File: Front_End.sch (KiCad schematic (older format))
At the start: 17 parts, among them SW2 JS202011SCQN, SW3 JS202011SCQN, U5 SKY65366-21, U6 BMI-S-101

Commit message: setup netclasses and added more footprints
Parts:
- RV1: footprint Resistors_SMD:R_0402 -> SFUSat-Radio:TC33_SMD
- SW2, SW3: footprint SFUSat-Radio:JS2020_SMD -> SFUSat-Radio:JS2020_TH
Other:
- note added: "RF Shield\n"
- note added: "Select external control of enable\n and VPC or tie internally to high \nor low respective."
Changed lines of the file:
@@
 F 0 "RV1" H 4650 5750 50  0000 C CNN
 F 1 "POT" H 4650 5850 50  0000 C CNN
-F 2 "Resistors_SMD:R_0402" H 4650 5850 50  0001 C CNN
+F 2 "SFUSat-Radio:TC33_SMD" H 4650 5850 50  0001 C CNN
 F 3 "" H 4650 5850 50  0000 C CNN
 	1    4650 5850
@@
 F 0 "SW2" H 3800 5750 60  0000 C CNN
 F 1 "JS202011SCQN" H 3600 6300 60  0000 C CNN
-F 2 "SFUSat-Radio:JS2020_SMD" H 3600 6150 60  0001 C CNN
+F 2 "SFUSat-Radio:JS2020_TH" H 3600 6150 60  0001 C CNN
 F 3 "" H 3600 6150 60  0000 C CNN
 	1    3600 6150
@@
 F 0 "SW3" H 6100 5750 60  0000 C CNN
 F 1 "JS202011SCQN" H 5900 6300 60  0000 C CNN
-F 2 "SFUSat-Radio:JS2020_SMD" H 5900 6150 60  0001 C CNN
+F 2 "SFUSat-Radio:JS2020_TH" H 5900 6150 60  0001 C CNN
 F 3 "" H 5900 6150 60  0000 C CNN
 	1    5900 6150
@@
 	8100 5000 8000 5000
 Connection ~ 8000 5000
+Text Notes 3000 7000 0    60   ~ 0
+Select external control of enable\n and VPC or tie internally to high \nor low respective.
+Text Notes 7500 5850 0    60   ~ 0
+RF Shield\n
 $EndSCHEMATC

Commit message: fixed filesystem
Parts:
- C28, C29, C30, L2: footprint (none) -> Capacitors_SMD:C_0402
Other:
- note added: "LNA and PA can be bypassed if\n BYP in pulled HIGH. Good as a \nkill switch to high power output.\n"
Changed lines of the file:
@@
 F 0 "C29" V 7300 3200 50  0000 C CNN
 F 1 "3pF" V 7600 3200 50  0000 C CNN
-F 2 "" H 7488 3050 50  0001 C CNN
+F 2 "Capacitors_SMD:C_0402" H 7488 3050 50  0001 C CNN
 F 3 "" H 7450 3200 50  0000 C CNN
 	1    7450 3200
@@
 F 0 "C28" H 7075 3450 50  0000 L CNN
 F 1 "8.2pF" H 7075 3250 50  0000 L CNN
-F 2 "" H 7088 3200 50  0001 C CNN
+F 2 "Capacitors_SMD:C_0402" H 7088 3200 50  0001 C CNN
 F 3 "" H 7050 3350 50  0000 C CNN
 	1    7050 3350
@@
 F 0 "C30" H 7875 3450 50  0000 L CNN
 F 1 "8.2pF" H 7875 3250 50  0000 L CNN
-F 2 "" H 7888 3200 50  0001 C CNN
+F 2 "Capacitors_SMD:C_0402" H 7888 3200 50  0001 C CNN
 F 3 "" H 7850 3350 50  0000 C CNN
 	1    7850 3350
@@
 F 0 "L2" V 7400 2825 50  0000 C CNN
 F 1 "12nH" V 7550 2825 50  0000 C CNN
-F 2 "" H 7450 2825 50  0001 C CNN
+F 2 "Capacitors_SMD:C_0402" H 7450 2825 50  0001 C CNN
 F 3 "" H 7450 2825 50  0000 C CNN
 	1    7450 2825
@@
 Text Label 2900 6400 0    60   ~ 0
 EN
-Text Notes 2600 4900 0    60   ~ 0
+Text Notes 2100 3600 0    60   ~ 0
 TR and BYP should not be \npulled high if EN is pulled low
 $Comp
@@
 Text Notes 7500 5850 0    60   ~ 0
 RF Shield\n
+Text Notes 5150 6850 0    60   ~ 0
+LNA and PA can be bypassed if\n BYP in pulled HIGH. Good as a \nkill switch to high power output.\n
 $EndSCHEMATC

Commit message: added some test points
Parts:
- removed SW2: JS202011SCQN, SFUSat-Radio:JS2020_TH, symbol JS202011SCQN
- added P? (x2): CONN_01X03, symbol CONN_01X03
- added W?: TEST_1P, symbol TEST_1P
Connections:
- wire segments 40 -> 41
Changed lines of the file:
@@
 Text HLabel 8200 3200 2    60   Input ~ 0
 ANT
-Text HLabel 4100 6100 2    60   Input ~ 0
+Text HLabel 4100 6400 2    60   Input ~ 0
 PA_ADJ
 Text HLabel 6500 4000 2    60   Input ~ 0
@@
 Wire Wire Line
 	4700 3350 3800 3350
-Text HLabel 4100 6350 2    60   Input ~ 0
+Text HLabel 3300 6400 2    60   Input ~ 0
 EN
 Text Notes 3400 2775 0    60   ~ 0
@@
 Text Label 3800 3700 0    60   ~ 0
 VPC
-Text Label 2900 6150 0    60   ~ 0
+Text Label 4350 6300 2    60   ~ 0
 VPC
 Text HLabel 4800 5850 2    60   Input ~ 0
@@
 	0    1    1    0
 $EndComp
-$Comp
-L JS202011SCQN SW2
-U 1 1 587E3043
-P 3600 6150
-F 0 "SW2" H 3800 5750 60  0000 C CNN
-F 1 "JS202011SCQN" H 3600 6300 60  0000 C CNN
-F 2 "SFUSat-Radio:JS2020_TH" H 3600 6150 60  0001 C CNN
-F 3 "" H 3600 6150 60  0000 C CNN
-	1    3600 6150
-	1    0    0    -1
-$EndComp
-Wire Wire Line
-	3100 6150 2900 6150
 Wire Wire Line
 	4650 6200 4100 6200
-Text HLabel 4100 6450 2    60   Input ~ 0
+Text HLabel 3300 6200 2    60   Input ~ 0
 3V3
 Text Label 3800 3350 0    60   ~ 0
 EN
-Wire Wire Line
-	3100 6400 2900 6400
-Text Label 2900 6400 0    60   ~ 0
+Text Label 3450 6300 2    60   ~ 0
 EN
 Text Notes 2100 3600 0    60   ~ 0
@@
 Text Notes 5150 6850 0    60   ~ 0
 LNA and PA can be bypassed if\n BYP in pulled HIGH. Good as a \nkill switch to high power output.\n
+$Comp
+L CONN_01X03 P?
+U 1 1 5881FCF5
+P 3900 6300
+F 0 "P?" H 3900 6500 50  0000 C CNN
+F 1 "CONN_01X03" V 4000 6300 50  0000 C CNN
+F 2 "" H 3900 6300 50  0000 C CNN
+F 3 "" H 3900 6300 50  0000 C CNN
+	1    3900 6300
+	-1   0    0    1
+$EndComp
+$Comp
+L CONN_01X03 P?
+U 1 1 5881FDBC
+P 3100 6300
+F 0 "P?" H 3100 6500 50  0000 C CNN
+F 1 "CONN_01X03" V 3200 6300 50  0000 C CNN
+F 2 "" H 3100 6300 50  0000 C CNN
+F 3 "" H 3100 6300 50  0000 C CNN
+	1    3100 6300
+	-1   0    0    1
+$EndComp
+Wire Wire Line
+	4100 6300 4350 6300
+Wire Wire Line
+	3300 6300 3450 6300
+$Comp
+L TEST_1P W?
+U 1 1 58821DE8
+P 4300 6050
+F 0 "W?" H 4300 6320 50  0000 C CNN
+F 1 "TEST_1P" H 4300 6250 50  0000 C CNN
+F 2 "" H 4500 6050 50  0000 C CNN
+F 3 "" H 4500 6050 50  0000 C CNN
+	1    4300 6050
+	1    0    0    -1
+$EndComp
+Wire Wire Line
+	4300 6050 4300 6200
+Connection ~ 4300 6200
 $EndSCHEMATC

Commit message: layed out all components
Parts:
- removed U6: BMI-S-101, SFUSat-Radio:BMI-S-101, symbol BMI-S-101
- P2, P3: renamed from P?; footprint (none) -> Socket_Strips:Socket_Strip_Straight_1x03
- W3: renamed from W?; footprint (none) -> Measurement_Points:Measurement_Point_Round-SMD-Pad_Small
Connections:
- wire segments 41 -> 37
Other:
- note removed: "RF Shield\n"
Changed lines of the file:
@@
 $EndComp
 $Comp
-L GND #PWR028
+L GND #PWR027
 U 1 1 58719F72
 P 5500 4650
-F 0 "#PWR028" H 5500 4400 50  0001 C CNN
+F 0 "#PWR027" H 5500 4400 50  0001 C CNN
 F 1 "GND" H 5500 4500 50  0000 C CNN
 F 2 "" H 5500 4650 50  0000 C CNN
@@
 $EndComp
 $Comp
-L GND #PWR029
+L GND #PWR028
 U 1 1 5871BAFA
 P 5750 2550
-F 0 "#PWR029" H 5750 2300 50  0001 C CNN
+F 0 "#PWR028" H 5750 2300 50  0001 C CNN
 F 1 "GND" H 5750 2400 50  0000 C CNN
 F 2 "" H 5750 2550 50  0000 C CNN
@@
 $EndComp
 $Comp
-L GND #PWR030
+L GND #PWR029
 U 1 1 5871BB16
 P 6050 2550
-F 0 "#PWR030" H 6050 2300 50  0001 C CNN
+F 0 "#PWR029" H 6050 2300 50  0001 C CNN
 F 1 "GND" H 6050 2400 50  0000 C CNN
 F 2 "" H 6050 2550 50  0000 C CNN
@@
 $EndComp
 $Comp
-L GND #PWR031
+L GND #PWR030
 U 1 1 5871BB32
 P 6350 2550
-F 0 "#PWR031" H 6350 2300 50  0001 C CNN
+F 0 "#PWR030" H 6350 2300 50  0001 C CNN
 F 1 "GND" H 6350 2400 50  0000 C CNN
 F 2 "" H 6350 2550 50  0000 C CNN
@@
 $EndComp
 $Comp
-L GND #PWR032
+L GND #PWR031
 U 1 1 5871BD81
 P 5150 2550
-F 0 "#PWR032" H 5150 2300 50  0001 C CNN
+F 0 "#PWR031" H 5150 2300 50  0001 C CNN
 F 1 "GND" H 5150 2400 50  0000 C CNN
 F 2 "" H 5150 2550 50  0000 C CNN
@@
 $EndComp
 $Comp
-L GND #PWR033
+L GND #PWR032
 U 1 1 5871BDA1
 P 4850 2550
-F 0 "#PWR033" H 4850 2300 50  0001 C CNN
+F 0 "#PWR032" H 4850 2300 50  0001 C CNN
 F 1 "GND" H 4850 2400 50  0000 C CNN
 F 2 "" H 4850 2550 50  0000 C CNN
@@
 	7050 2825 7050 3200
 $Comp
-L GND #PWR034
+L GND #PWR033
 U 1 1 5871C376
 P 7050 3600
-F 0 "#PWR034" H 7050 3350 50  0001 C CNN
+F 0 "#PWR033" H 7050 3350 50  0001 C CNN
 F 1 "GND" H 7050 3450 50  0000 C CNN
 F 2 "" H 7050 3600 50  0000 C CNN
@@
 $EndComp
 $Comp
-L GND #PWR035
+L GND #PWR034
 U 1 1 5871C39E
 P 7850 3600
-F 0 "#PWR035" H 7850 3350 50  0001 C CNN
+F 0 "#PWR034" H 7850 3350 50  0001 C CNN
 F 1 "GND" H 7850 3450 50  0000 C CNN
 F 2 "" H 7850 3600 50  0000 C CNN
@@
 $EndComp
 $Comp
-L GND #PWR036
+L GND #PWR035
 U 1 1 5871CA19
 P 4500 4400
-F 0 "#PWR036" H 4500 4150 50  0001 C CNN
+F 0 "#PWR035" H 4500 4150 50  0001 C CNN
 F 1 "GND" H 4500 4250 50  0000 C CNN
 F 2 "" H 4500 4400 50  0000 C CNN
@@
 $EndComp
 $Comp
-L GND #PWR037
+L GND #PWR036
 U 1 1 5871CD23
 P 4150 4050
-F 0 "#PWR037" H 4150 3800 50  0001 C CNN
+F 0 "#PWR036" H 4150 3800 50  0001 C CNN
 F 1 "GND" H 4150 3900 50  0000 C CNN
 F 2 "" H 4150 4050 50  0000 C CNN
@@
 $EndComp
 $Comp
-L GND #PWR038
+L GND #PWR037
 U 1 1 587C3C45
 P 4650 6600
-F 0 "#PWR038" H 4650 6350 50  0001 C CNN
+F 0 "#PWR037" H 4650 6350 50  0001 C CNN
 F 1 "GND" H 4650 6450 50  0000 C CNN
 F 2 "" H 4650 6600 50  0000 C CNN
@@
 3V3
 $Comp
-L GND #PWR039
+L GND #PWR038
 U 1 1 58829BDE
 P 6400 6100
-F 0 "#PWR039" H 6400 5850 50  0001 C CNN
+F 0 "#PWR038" H 6400 5850 50  0001 C CNN
 F 1 "GND" H 6400 5950 50  0000 C CNN
 F 2 "" H 6400 6100 50  0000 C CNN
@@
 	0    -1   -1   0
 $EndComp
-$Comp
-L BMI-S-101 U6
-U 1 1 5882B6C7
-P 7600 4850
-F 0 "U6" H 7750 4050 60  0000 C CNN
-F 1 "BMI-S-101" H 7600 5000 60  0000 C CNN
-F 2 "SFUSat-Radio:BMI-S-101" H 7600 4850 60  0001 C CNN
-F 3 "" H 7600 4850 60  0000 C CNN
-	1    7600 4850
-	1    0    0    -1
-$EndComp
-$Comp
-L GND #PWR040
-U 1 1 5882B8A8
-P 8100 5000
-F 0 "#PWR040" H 8100 4750 50  0001 C CNN
-F 1 "GND" H 8100 4850 50  0000 C CNN
-F 2 "" H 8100 5000 50  0000 C CNN
-F 3 "" H 8100 5000 50  0000 C CNN
-	1    8100 5000
-	0    -1   -1   0
-$EndComp
-Wire Wire Line
-	8000 4850 8000 5550
-Wire Wire Line
-	8000 4950 8000 5250
-Connection ~ 8000 5050
-Connection ~ 8000 4950
-Connection ~ 8000 5150
-Connection ~ 8000 5250
-Wire Wire Line
-	8000 5350 8000 5450
-Connection ~ 8000 5450
-Connection ~ 8000 5350
-Wire Wire Line
-	8100 5000 8000 5000
-Connection ~ 8000 5000
 Text Notes 3000 7000 0    60   ~ 0
 Select external control of enable\n and VPC or tie internally to high \nor low respective.
-Text Notes 7500 5850 0    60   ~ 0
-RF Shield\n
 Text Notes 5150 6850 0    60   ~ 0
 LNA and PA can be bypassed if\n BYP in pulled HIGH. Good as a \nkill switch to high power output.\n
 $Comp
-L CONN_01X03 P?
+L CONN_01X03 P3
 U 1 1 5881FCF5
 P 3900 6300
-F 0 "P?" H 3900 6500 50  0000 C CNN
+F 0 "P3" H 3900 6500 50  0000 C CNN
 F 1 "CONN_01X03" V 4000 6300 50  0000 C CNN
-F 2 "" H 3900 6300 50  0000 C CNN
+F 2 "Socket_Strips:Socket_Strip_Straight_1x03" H 3900 6300 50  0001 C CNN
 F 3 "" H 3900 6300 50  0000 C CNN
 	1    3900 6300
@@
 $EndComp
 $Comp
-L CONN_01X03 P?
+L CONN_01X03 P2
 U 1 1 5881FDBC
 P 3100 6300
-F 0 "P?" H 3100 6500 50  0000 C CNN
+F 0 "P2" H 3100 6500 50  0000 C CNN
 F 1 "CONN_01X03" V 3200 6300 50  0000 C CNN
-F 2 "" H 3100 6300 50  0000 C CNN
+F 2 "Socket_Strips:Socket_Strip_Straight_1x03" H 3100 6300 50  0001 C CNN
 F 3 "" H 3100 6300 50  0000 C CNN
 	1    3100 6300
@@
 	3300 6300 3450 6300
 $Comp
-L TEST_1P W?
+L TEST_1P W3
 U 1 1 58821DE8
 P 4300 6050
-F 0 "W?" H 4300 6320 50  0000 C CNN
+F 0 "W3" H 4300 6320 50  0000 C CNN
 F 1 "TEST_1P" H 4300 6250 50  0000 C CNN
-F 2 "" H 4500 6050 50  0000 C CNN
+F 2 "Measurement_Points:Measurement_Point_Round-SMD-Pad_Small" H 4500 6050 50  0001 C CNN
 F 3 "" H 4500 6050 50  0000 C CNN
 	1    4300 6050

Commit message: Checked changes from botched commit
-R5 and R6 are gone as desired
-C4 changed from 10 nF to 100 nF looks good
-Split up nets between pins 27 and 28 so each have their own dedicated
capacitor
-Added C9 to pin 28 and forward annotated it into the layout
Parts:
- RV1: symbol POT -> POT-RESCUE-SFUSat-Radio
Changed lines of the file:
@@
 EESchema Schematic File Version 2
+LIBS:SFUSat-Radio-rescue
 LIBS:power
 LIBS:device
@@
 $EndComp
 $Comp
-L GND #PWR027
+L GND #PWR32
 U 1 1 58719F72
 P 5500 4650
-F 0 "#PWR027" H 5500 4400 50  0001 C CNN
+F 0 "#PWR32" H 5500 4400 50  0001 C CNN
 F 1 "GND" H 5500 4500 50  0000 C CNN
 F 2 "" H 5500 4650 50  0000 C CNN
@@
 $EndComp
 $Comp
-L GND #PWR028
+L GND #PWR33
 U 1 1 5871BAFA
 P 5750 2550
-F 0 "#PWR028" H 5750 2300 50  0001 C CNN
+F 0 "#PWR33" H 5750 2300 50  0001 C CNN
 F 1 "GND" H 5750 2400 50  0000 C CNN
 F 2 "" H 5750 2550 50  0000 C CNN
@@
 $EndComp
 $Comp
-L GND #PWR029
+L GND #PWR34
 U 1 1 5871BB16
 P 6050 2550
-F 0 "#PWR029" H 6050 2300 50  0001 C CNN
+F 0 "#PWR34" H 6050 2300 50  0001 C CNN
 F 1 "GND" H 6050 2400 50  0000 C CNN
 F 2 "" H 6050 2550 50  0000 C CNN
@@
 $EndComp
 $Comp
-L GND #PWR030
+L GND #PWR35
 U 1 1 5871BB32
 P 6350 2550
-F 0 "#PWR030" H 6350 2300 50  0001 C CNN
+F 0 "#PWR35" H 6350 2300 50  0001 C CNN
 F 1 "GND" H 6350 2400 50  0000 C CNN
 F 2 "" H 6350 2550 50  0000 C CNN
@@
 $EndComp
 $Comp
-L GND #PWR031
+L GND #PWR31
 U 1 1 5871BD81
 P 5150 2550
-F 0 "#PWR031" H 5150 2300 50  0001 C CNN
+F 0 "#PWR31" H 5150 2300 50  0001 C CNN
 F 1 "GND" H 5150 2400 50  0000 C CNN
 F 2 "" H 5150 2550 50  0000 C CNN
@@
 $EndComp
 $Comp
-L GND #PWR032
+L GND #PWR30
 U 1 1 5871BDA1
 P 4850 2550
-F 0 "#PWR032" H 4850 2300 50  0001 C CNN
+F 0 "#PWR30" H 4850 2300 50  0001 C CNN
 F 1 "GND" H 4850 2400 50  0000 C CNN
 F 2 "" H 4850 2550 50  0000 C CNN
@@
 	7050 2825 7050 3200
 $Comp
-L GND #PWR033
+L GND #PWR37
 U 1 1 5871C376
 P 7050 3600
-F 0 "#PWR033" H 7050 3350 50  0001 C CNN
+F 0 "#PWR37" H 7050 3350 50  0001 C CNN
 F 1 "GND" H 7050 3450 50  0000 C CNN
 F 2 "" H 7050 3600 50  0000 C CNN
@@
 $EndComp
 $Comp
-L GND #PWR034
+L GND #PWR38
 U 1 1 5871C39E
 P 7850 3600
-F 0 "#PWR034" H 7850 3350 50  0001 C CNN
+F 0 "#PWR38" H 7850 3350 50  0001 C CNN
 F 1 "GND" H 7850 3450 50  0000 C CNN
 F 2 "" H 7850 3600 50  0000 C CNN
@@
 $EndComp
 $Comp
-L GND #PWR035
+L GND #PWR28
 U 1 1 5871CA19
 P 4500 4400
-F 0 "#PWR035" H 4500 4150 50  0001 C CNN
+F 0 "#PWR28" H 4500 4150 50  0001 C CNN
 F 1 "GND" H 4500 4250 50  0000 C CNN
 F 2 "" H 4500 4400 50  0000 C CNN
@@
 $EndComp
 $Comp
-L GND #PWR036
+L GND #PWR27
 U 1 1 5871CD23
 P 4150 4050
-F 0 "#PWR036" H 4150 3800 50  0001 C CNN
+F 0 "#PWR27" H 4150 3800 50  0001 C CNN
 F 1 "GND" H 4150 3900 50  0000 C CNN
 F 2 "" H 4150 4050 50  0000 C CNN
@@
 $EndComp
 $Comp
-L GND #PWR037
+L GND #PWR29
 U 1 1 587C3C45
 P 4650 6600
-F 0 "#PWR037" H 4650 6350 50  0001 C CNN
+F 0 "#PWR29" H 4650 6350 50  0001 C CNN
 F 1 "GND" H 4650 6450 50  0000 C CNN
 F 2 "" H 4650 6600 50  0000 C CNN
@@
 3V3
 $Comp
-L POT RV1
+L POT-RESCUE-SFUSat-Radio RV1
 U 1 1 587CA745
 P 4650 5850
@@
 3V3
 $Comp
-L GND #PWR038
+L GND #PWR36
 U 1 1 58829BDE
 P 6400 6100
-F 0 "#PWR038" H 6400 5850 50  0001 C CNN
+F 0 "#PWR36" H 6400 5850 50  0001 C CNN
 F 1 "GND" H 6400 5950 50  0000 C CNN
 F 2 "" H 6400 6100 50  0000 C CNN

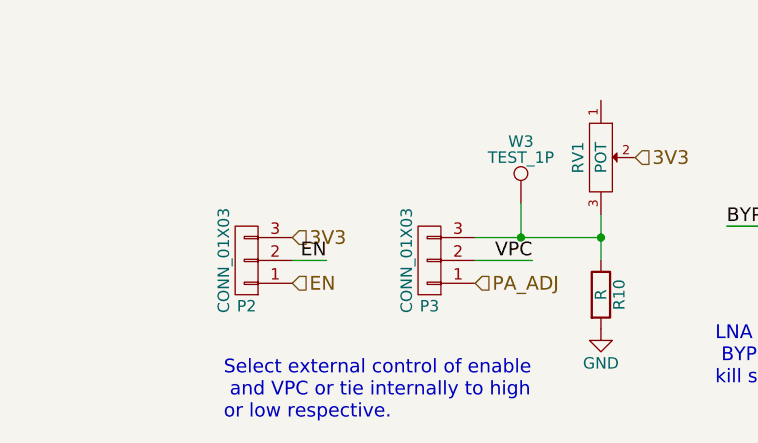
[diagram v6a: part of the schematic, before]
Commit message: added power connector, nets connected in layout
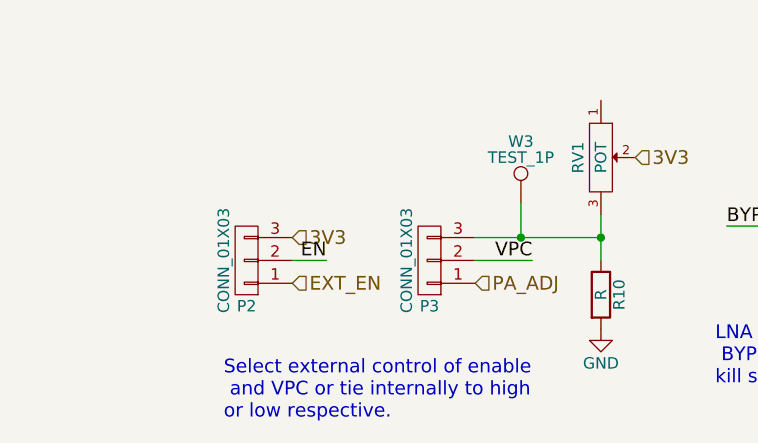
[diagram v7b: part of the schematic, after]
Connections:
- net EN: no longer P2.1 (P1)
- new net EXT_EN: P2.1 (P1)
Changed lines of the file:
@@
 $EndComp
 $Comp
-L GND #PWR026
+L GND #PWR027
 U 1 1 58719F72
 P 5500 4650
-F 0 "#PWR026" H 5500 4400 50  0001 C CNN
+F 0 "#PWR027" H 5500 4400 50  0001 C CNN
 F 1 "GND" H 5500 4500 50  0000 C CNN
 F 2 "" H 5500 4650 50  0000 C CNN
@@
 $EndComp
 $Comp
-L GND #PWR027
+L GND #PWR028
 U 1 1 5871BAFA
 P 5750 2550
-F 0 "#PWR027" H 5750 2300 50  0001 C CNN
+F 0 "#PWR028" H 5750 2300 50  0001 C CNN
 F 1 "GND" H 5750 2400 50  0000 C CNN
 F 2 "" H 5750 2550 50  0000 C CNN
@@
 $EndComp
 $Comp
-L GND #PWR028
+L GND #PWR029
 U 1 1 5871BB16
 P 6050 2550
-F 0 "#PWR028" H 6050 2300 50  0001 C CNN
+F 0 "#PWR029" H 6050 2300 50  0001 C CNN
 F 1 "GND" H 6050 2400 50  0000 C CNN
 F 2 "" H 6050 2550 50  0000 C CNN
@@
 $EndComp
 $Comp
-L GND #PWR029
+L GND #PWR030
 U 1 1 5871BB32
 P 6350 2550
-F 0 "#PWR029" H 6350 2300 50  0001 C CNN
+F 0 "#PWR030" H 6350 2300 50  0001 C CNN
 F 1 "GND" H 6350 2400 50  0000 C CNN
 F 2 "" H 6350 2550 50  0000 C CNN
@@
 $EndComp
 $Comp
-L GND #PWR030
+L GND #PWR031
 U 1 1 5871BD81
 P 5150 2550
-F 0 "#PWR030" H 5150 2300 50  0001 C CNN
+F 0 "#PWR031" H 5150 2300 50  0001 C CNN
 F 1 "GND" H 5150 2400 50  0000 C CNN
 F 2 "" H 5150 2550 50  0000 C CNN
@@
 $EndComp
 $Comp
-L GND #PWR031
+L GND #PWR032
 U 1 1 5871BDA1
 P 4850 2550
-F 0 "#PWR031" H 4850 2300 50  0001 C CNN
+F 0 "#PWR032" H 4850 2300 50  0001 C CNN
 F 1 "GND" H 4850 2400 50  0000 C CNN
 F 2 "" H 4850 2550 50  0000 C CNN
@@
 	7050 2825 7050 3200
 $Comp
-L GND #PWR032
+L GND #PWR033
 U 1 1 5871C376
 P 7050 3600
-F 0 "#PWR032" H 7050 3350 50  0001 C CNN
+F 0 "#PWR033" H 7050 3350 50  0001 C CNN
 F 1 "GND" H 7050 3450 50  0000 C CNN
 F 2 "" H 7050 3600 50  0000 C CNN
@@
 $EndComp
 $Comp
-L GND #PWR033
+L GND #PWR034
 U 1 1 5871C39E
 P 7850 3600
-F 0 "#PWR033" H 7850 3350 50  0001 C CNN
+F 0 "#PWR034" H 7850 3350 50  0001 C CNN
 F 1 "GND" H 7850 3450 50  0000 C CNN
 F 2 "" H 7850 3600 50  0000 C CNN
@@
 $EndComp
 $Comp
-L GND #PWR034
+L GND #PWR035
 U 1 1 5871CA19
 P 4500 4400
-F 0 "#PWR034" H 4500 4150 50  0001 C CNN
+F 0 "#PWR035" H 4500 4150 50  0001 C CNN
 F 1 "GND" H 4500 4250 50  0000 C CNN
 F 2 "" H 4500 4400 50  0000 C CNN
@@
 $EndComp
 $Comp
-L GND #PWR035
+L GND #PWR036
 U 1 1 5871CD23
 P 4150 4050
-F 0 "#PWR035" H 4150 3800 50  0001 C CNN
+F 0 "#PWR036" H 4150 3800 50  0001 C CNN
 F 1 "GND" H 4150 3900 50  0000 C CNN
 F 2 "" H 4150 4050 50  0000 C CNN
@@
 	4700 3350 3800 3350
 Text HLabel 3300 6400 2    60   Input ~ 0
-EN
+EXT_EN
 Text Notes 3400 2775 0    60   ~ 0
 TRX_SIG
@@
 $EndComp
 $Comp
-L GND #PWR036
+L GND #PWR037
 U 1 1 587C3C45
 P 4650 6600
-F 0 "#PWR036" H 4650 6350 50  0001 C CNN
+F 0 "#PWR037" H 4650 6350 50  0001 C CNN
 F 1 "GND" H 4650 6450 50  0000 C CNN
 F 2 "" H 4650 6600 50  0000 C CNN
@@
 3V3
 $Comp
-L GND #PWR037
+L GND #PWR038
 U 1 1 58829BDE
 P 6400 6100
-F 0 "#PWR037" H 6400 5850 50  0001 C CNN
+F 0 "#PWR038" H 6400 5850 50  0001 C CNN
 F 1 "GND" H 6400 5950 50  0000 C CNN
 F 2 "" H 6400 6100 50  0000 C CNN
